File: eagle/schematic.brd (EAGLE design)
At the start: 44.1 x 45.7 mm, 35 parts, among them U1 PIC18F252-I/SP

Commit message: PCB completed
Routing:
- net RA6: track 0.00 -> 34.9 mm, vias 0 -> 2
- net RA7: track 0.00 -> 29.4 mm, vias 0 -> 3
- net RA4: track 0.00 -> 29.0 mm, vias 0 -> 2
- net RA3: track 0.00 -> 26.5 mm, vias 0 -> 2
- net RC1: track 0.00 -> 26.2 mm, vias 0 -> 1
- net RB0: track 0.00 -> 25.7 mm, vias 0 -> 1
- net RA5: track 0.00 -> 25.2 mm, vias 0 -> 1
- net RC0: track 0.00 -> 24.5 mm
- net RB1: track 0.00 -> 19.2 mm, vias 0 -> 1
- net RC2: track 0.00 -> 19.1 mm
- net RC3: track 0.00 -> 18.7 mm
- net AN0: track 2.29 -> 20.9 mm
- net RB2: track 0.00 -> 12.9 mm
- net VDD: track 47.6 -> 58.8 mm
- net RC7: track 0.00 -> 10.8 mm
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- added copper zone on layer 1, net GND
- added copper zone on layer 16, net GND
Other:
- board text added: "*"
- board text added: "+"
- board text added: "-"
- board text added: "Binary Clock Version 0.1.0 Michel Lavoie 2016-11-26"

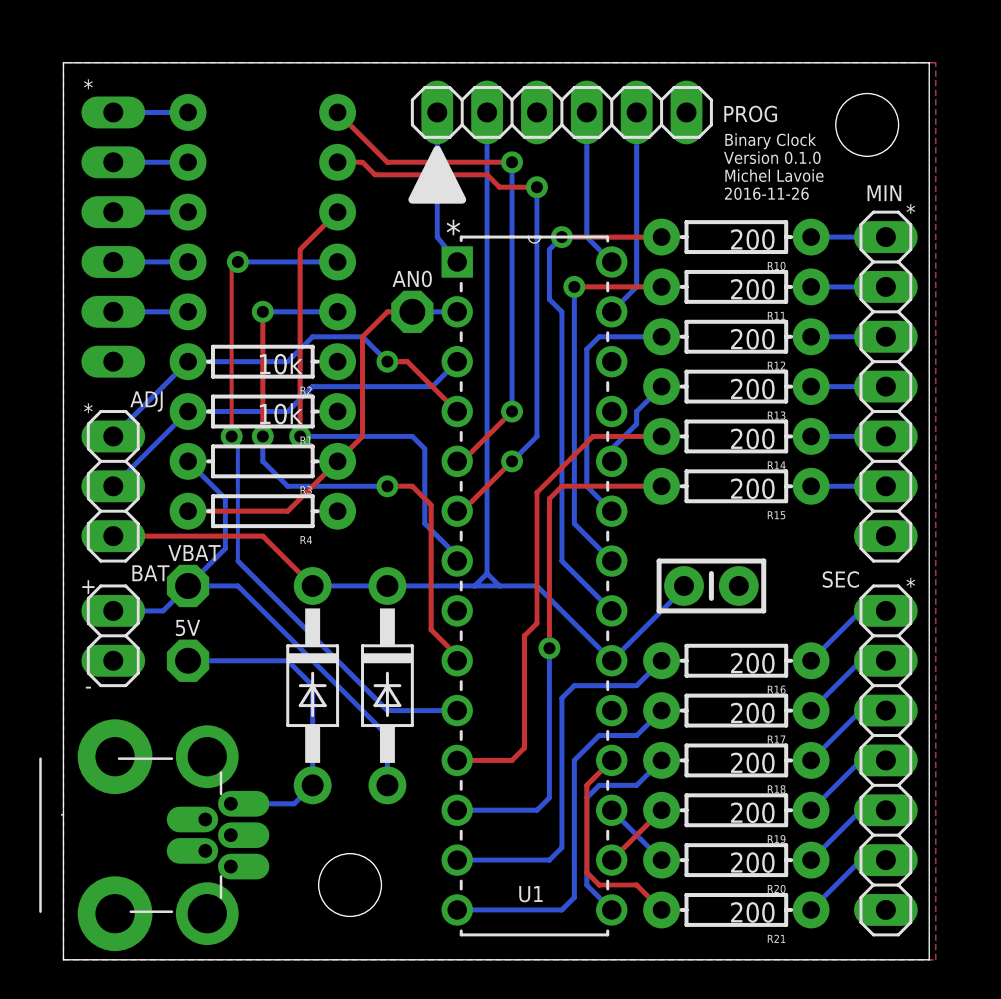
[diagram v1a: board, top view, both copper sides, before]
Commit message: Version 0.1.1. Applied all items in the To Do list.
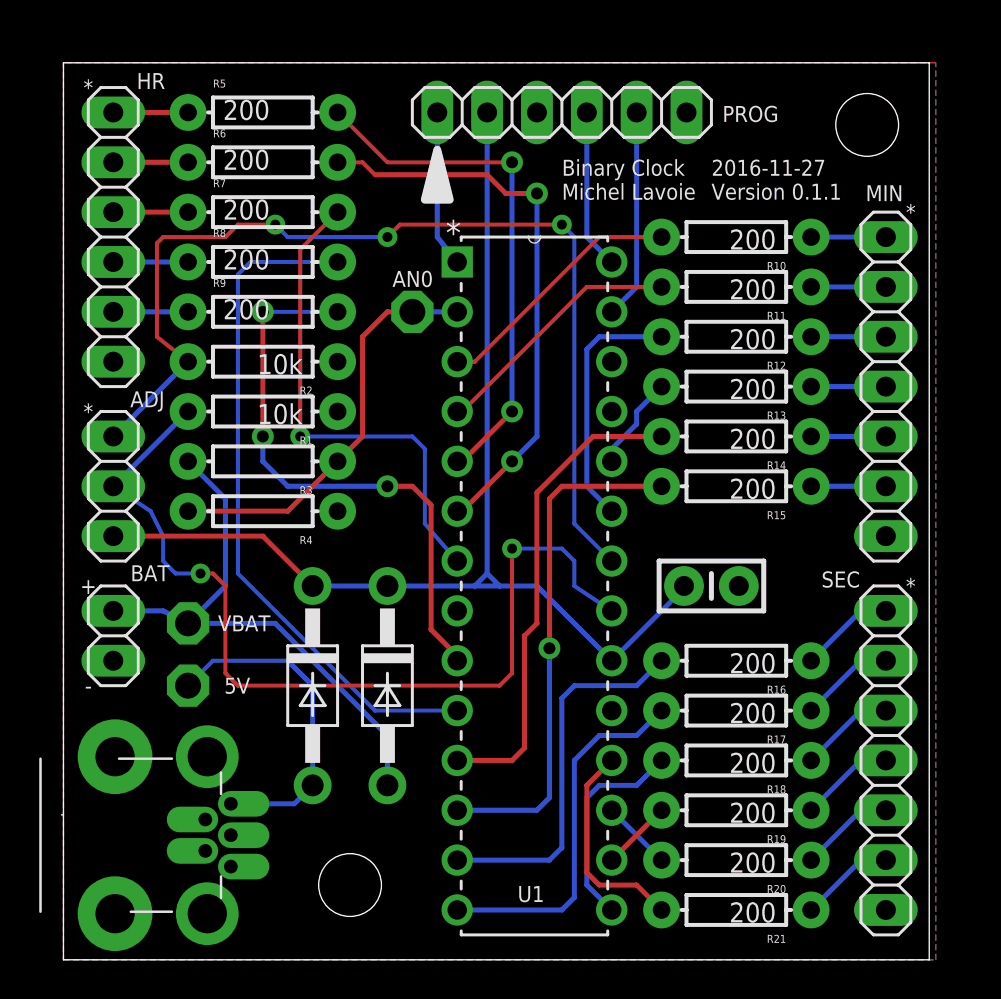
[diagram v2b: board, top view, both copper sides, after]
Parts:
- moved VBAT 1.91 mm to (6.35, 17.1)
- moved 5V 1.27 mm to (6.35, 14.0)
- flipped HR to the top
- flipped R5 to the top, turned to 0 degrees
- flipped R6 to the top, turned to 0 degrees
- flipped R7 to the top, turned to 0 degrees
- flipped R8 to the top, turned to 0 degrees
- flipped R9 to the top, turned to 0 degrees
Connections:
- net RA3 renamed HR0
- net RA4 renamed HR1
- net RA5 renamed HR2
- net RA6 renamed HR3
- net RA7 renamed HR4
- net RB2 renamed MIN2
- net RB3 renamed MIN3
- net RC0 renamed MIN4
- net RC1 renamed MIN5
- net RC2 renamed SEC0
- net RC3 renamed SEC1
- net RC4 renamed SEC2
- net RC5 renamed SEC3
- net RC6 renamed SEC4
- net RC7 renamed SEC5
- removed net RB0: R10.P$2, U1.21
- removed net RB1: R11.P$2, U1.22
- new net MIN0: R10.P$2, U1.3
- new net MIN1: R11.P$2, U1.4
- net ADJ-HR: now also U1.21; no longer U1.3
- net ADJ-MIN: now also U1.22; no longer U1.4
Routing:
- net ADJ-MIN: track 21.2 -> 51.9 mm, vias 1 -> 3
- net ADJ-HR: track 20.2 -> 47.0 mm, vias 0 -> 2
- net RB0: track 25.7 -> 0.00 mm, vias 1 -> 0
- net RB1: track 19.2 -> 0.00 mm, vias 1 -> 0
- net MIN1: track 0.00 -> 13.0 mm
- net MIN0: track 0.00 -> 13.0 mm
- net VBAT: track 28.1 -> 28.9 mm
- net 5V: track 16.5 -> 17.0 mm
- net HR3: track 34.9 -> 34.7 mm, vias 2 -> 0
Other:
- board text added: "2016-11-27 Version 0.1.1"
- board text added: "Binary Clock Michel Lavoie"
- board text removed: "Binary Clock Version 0.1.0 Michel Lavoie 2016-11-26"
